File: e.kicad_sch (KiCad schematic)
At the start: 10 parts, among them SW1 usr, SW2 rst, U1 Display_ST7789, U2 MAX98357A

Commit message: Updated footprint library path for custom footprints
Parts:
- LS1: footprint stupid-dumb-speaker:stupid-dumb-speaker -> custom-fp:stupid-dumb-speaker
- U1: footprint display-lol:display-lol -> custom-fp:display-lol
- U2: footprint amp-of-doom:MAX98357A -> custom-fp:MAX98357A
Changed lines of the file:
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@@
 			)
 		)
-		(property "Footprint" "stupid-dumb-speaker:stupid-dumb-speaker"
+		(property "Footprint" "custom-fp:stupid-dumb-speaker"
 			(at 163.83 147.32 0)
 			(hide yes)
@@
 			)
 		)
-		(property "Footprint" "amp-of-doom:MAX98357A"
+		(property "Footprint" "custom-fp:MAX98357A"
 			(at 140.97 152.4 0)
 			(hide yes)
@@
 			)
 		)
-		(property "Footprint" "display-lol:display-lol"
+		(property "Footprint" "custom-fp:display-lol"
 			(at 92.71 93.98 0)
 			(hide yes)

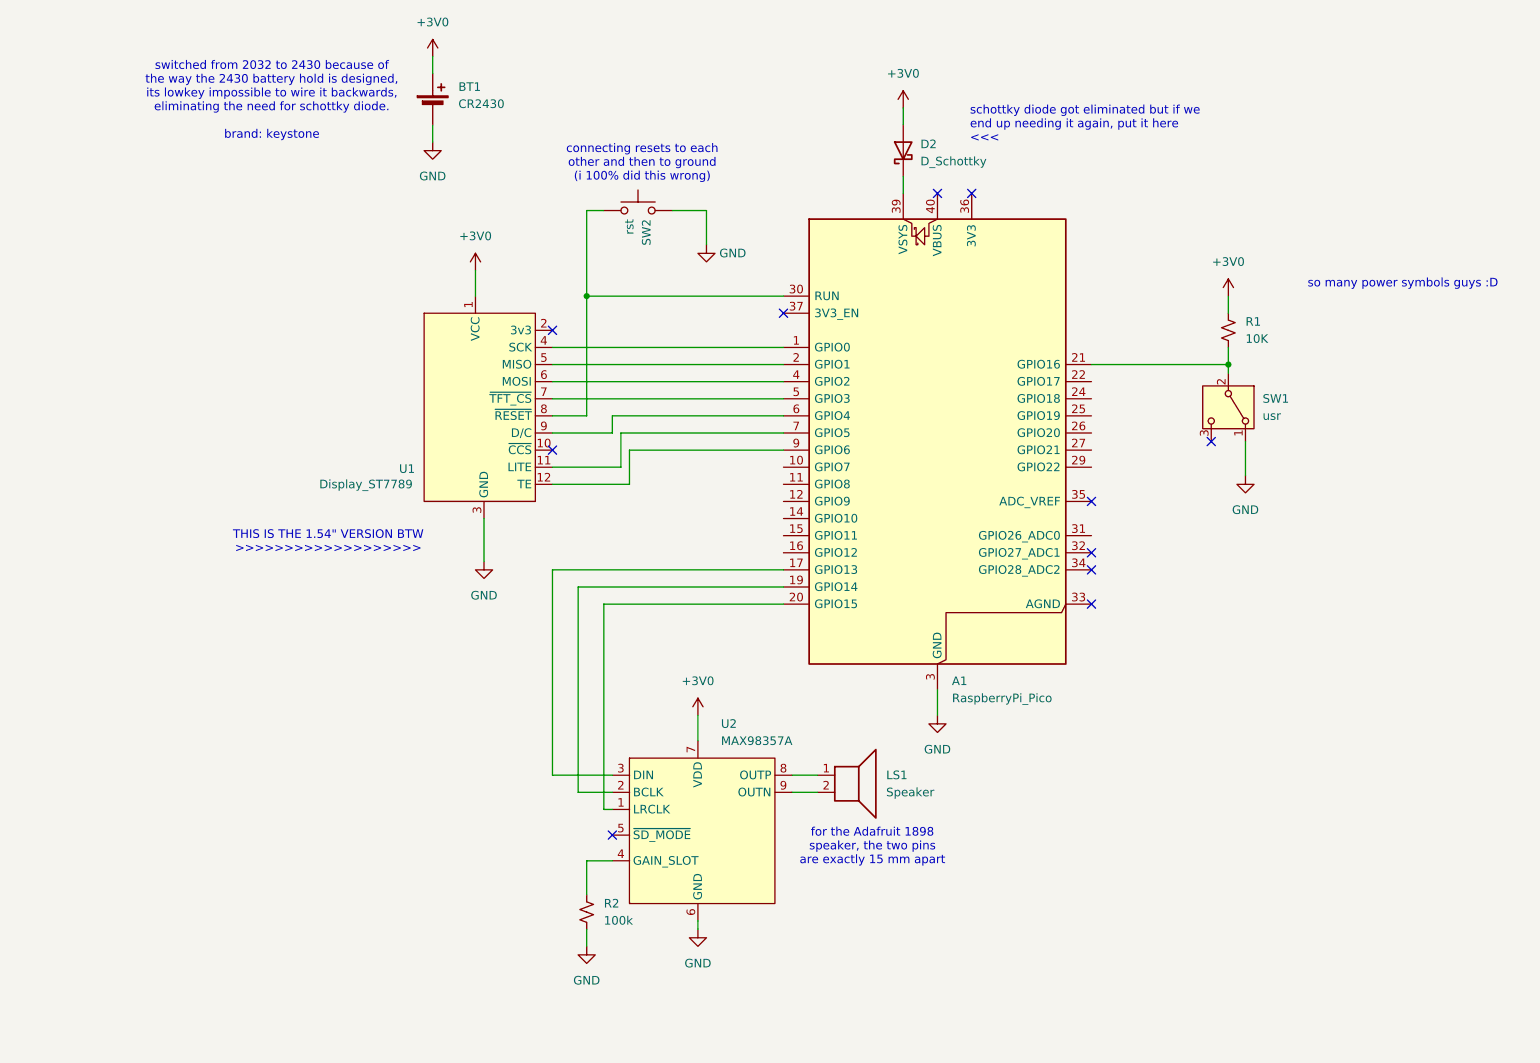
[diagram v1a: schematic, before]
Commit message: fixed some ERC/DRC errors
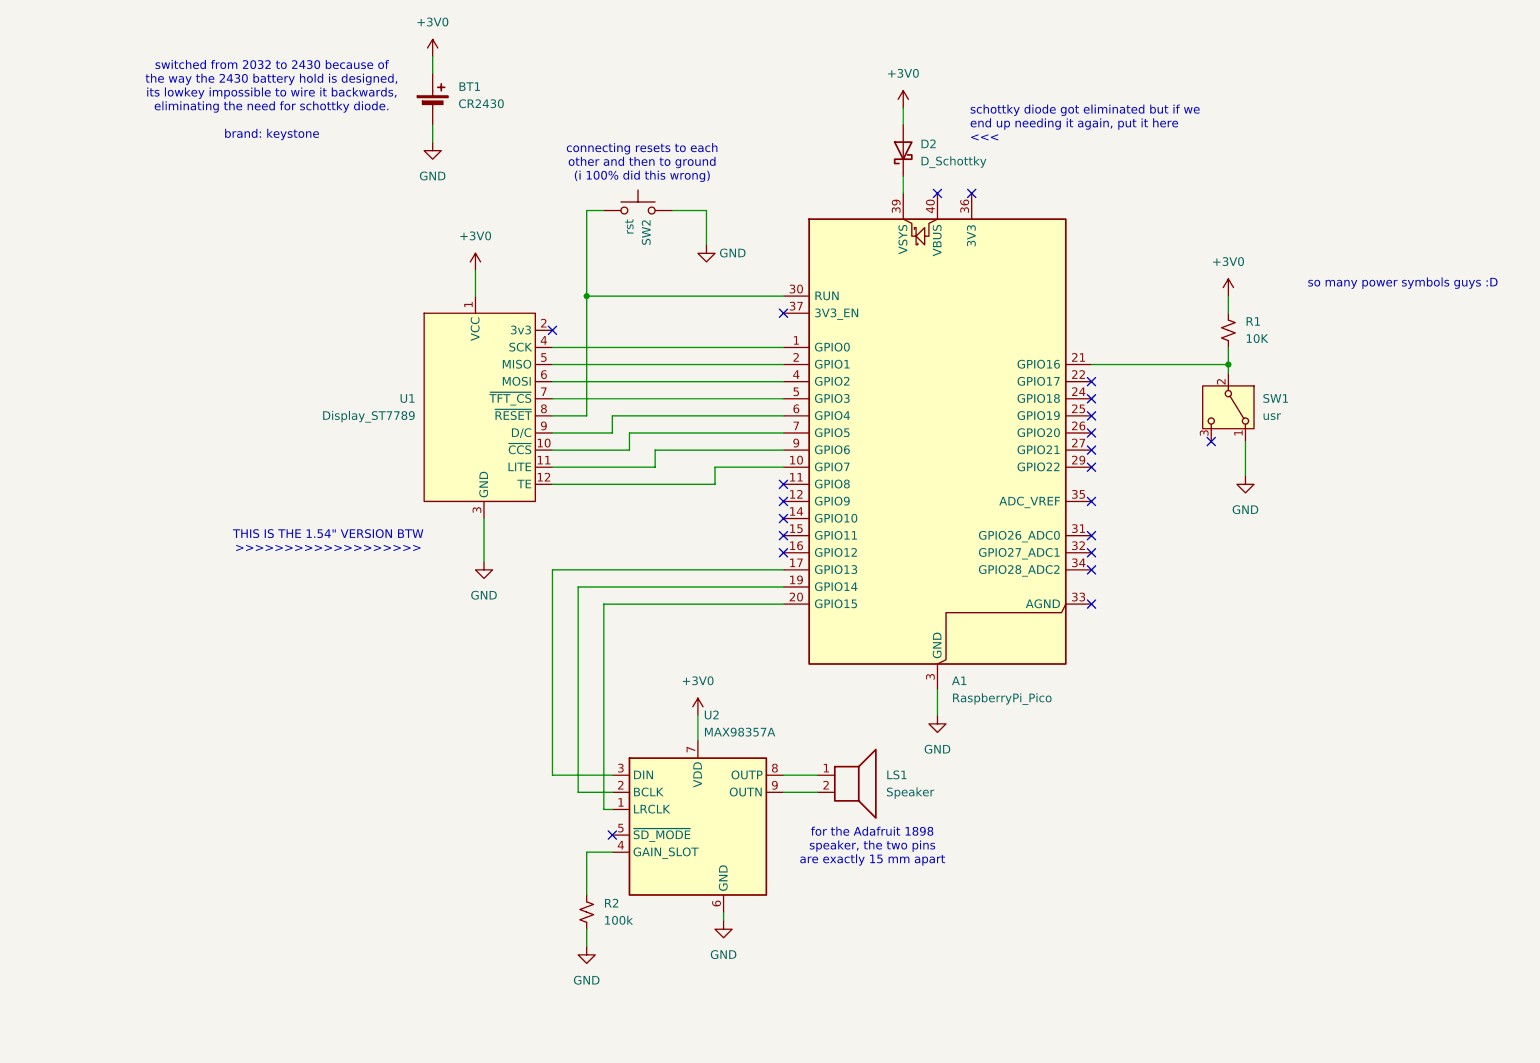
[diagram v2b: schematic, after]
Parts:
- removed U1: Display_ST7789, custom-fp:display-lol, symbol display_idk_lol:small-display
- added U1: Display_ST7789, custom-fp:display-lol, symbol cool-stuff:small-display
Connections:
- net +3V0: now also U1.1 (VCC)
- net GND: now also U1.3 (GND)
- net at A1.1 (GPIO0): now also U1.4 (SCK)
- net at A1.10 (GPIO7): now also U1.12 (TE)
- net at A1.2 (GPIO1): now also U1.5 (MISO)
- net at A1.30 (RUN), SW2.1: now also U1.8 (~{RESET})
- net at A1.4 (GPIO2): now also U1.6 (MOSI)
- net at A1.5 (GPIO3): now also U1.7 (~{TFT_CS})
- net at A1.6 (GPIO4): now also U1.9 (D/C)
- net at A1.7 (GPIO5): now also U1.10 (~{CCS})
- net at A1.9 (GPIO6): now also U1.11 (LITE)
- no-connect marks 11 -> 22
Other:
- moved on the sheet: U2

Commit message: wowwwww
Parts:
- removed SW1: usr, Button_Switch_THT:SW_Slide_SPDT_Straight_CK_OS102011MS2Q, symbol Switch:SW_SPDT
- removed U1: Display_ST7789, custom-fp:display-lol, symbol cool-stuff:small-display
- added SW1: usr, Button_Switch_SMD:SW_SPST_B3S-1000, symbol Switch:SW_Push
- added U1: (no value), display-lol:display-lol, symbol display_idk_lol:small-display
- LS1: footprint custom-fp:stupid-dumb-speaker -> stupid-dumb-speaker:stupid-dumb-speaker
- U2: footprint custom-fp:MAX98357A -> Package_DFN_QFN:TQFN-16-1EP_3x3mm_P0.5mm_EP1.23x1.23mm
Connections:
- net +3V0: now also U2.8 (OUTP), U1.1 (VCC)
- net GND: now also SW2.1, U2.11 (GND), U2.15 (GND), SW1.2, U1.3 (GND); no longer SW2.2
- net at A1.20 (GPIO15): no longer U2.1 (LRCLK)
- net at A1.19 (GPIO14): no longer U2.2 (BCLK)
- net at U2.3 (DIN): now also A1.1 (GPIO0); no longer A1.17 (GPIO13)
- net at A1.2 (GPIO1): now also U2.2 (BCLK)
- net at A1.21 (GPIO16), R1.2: now also SW1.1
- net at A1.22 (GPIO17): now also U1.4 (SCK)
- net at A1.24 (GPIO18): now also U1.5 (MISO)
- net at A1.25 (GPIO19): now also U1.6 (MOSI)
- net at A1.26 (GPIO20): now also U1.7 (~{TFT_CS})
- net at A1.27 (GPIO21): now also U1.9 (D/C)
- net at A1.29 (GPIO22): now also U1.11 (LITE)
- net at A1.30 (RUN): now also SW2.2, U1.8 (~{RESET}); no longer SW2.1
- net at A1.4 (GPIO2): now also U2.1 (LRCLK)
- no-connect marks 22 -> 24
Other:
- note added: "THIS IS THE 1.54" VERSION BTW <<<<<<<<<<<<<<<<<<<"
- note removed: "THIS IS THE 1.54" VERSION BTW >>>>>>>>>>>>>>>>>>>"
- moved on the sheet: A1, BT1, D2, LS1, R1, R2

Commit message: omg yay pcb fully made and its amazing and beautiful and the DRC errors make no sense :3
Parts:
- removed SW1: usr, Button_Switch_SMD:SW_SPST_B3S-1000, symbol Switch:SW_Push
- added SW1: usr, Button_Switch_THT:SW_Slide_SPDT_Straight_CK_OS102011MS2Q, symbol Switch:SW_SPDT
- U1: value (none) -> Display_ST7789
- U2: footprint Package_DFN_QFN:TQFN-16-1EP_3x3mm_P0.5mm_EP1.23x1.23mm -> MAX98357A:MAX98357A
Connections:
- net +3V0: no longer U2.8 (OUTP)
- net GND: now also SW1.1 (A); no longer U2.11 (GND), U2.15 (GND)
- net at A1.21 (GPIO16), R1.2: now also SW1.2 (B)
- no-connect marks 24 -> 25

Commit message: fixed so many things (i hope)
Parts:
- U2: footprint MAX98357A:MAX98357A -> amp-of-doom:MAX98357A
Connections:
- net GND: now also SW2.2; no longer SW2.1
- net at U2.1 (LRCLK): now also A1.20 (GPIO15); no longer A1.4 (GPIO2)
- net at U2.2 (BCLK): now also A1.19 (GPIO14); no longer A1.2 (GPIO1)
- net at U2.3 (DIN): now also A1.17 (GPIO13); no longer A1.1 (GPIO0)
- net at U1.4 (SCK): now also A1.1 (GPIO0); no longer A1.22 (GPIO17)
- net at U1.5 (MISO): now also A1.2 (GPIO1); no longer A1.24 (GPIO18)
- net at A1.25 (GPIO19): no longer U1.6 (MOSI)
- net at A1.26 (GPIO20): no longer U1.7 (~{TFT_CS})
- net at A1.27 (GPIO21): no longer U1.9 (D/C)
- net at A1.29 (GPIO22): no longer U1.11 (LITE)
- net at A1.30 (RUN), U1.8 (~{RESET}): now also SW2.1; no longer SW2.2
- net at A1.5 (GPIO3): now also U1.7 (~{TFT_CS})
- net at A1.6 (GPIO4): now also U1.9 (D/C)
- net at A1.7 (GPIO5): now also U1.11 (LITE)
- net at A1.9 (GPIO6): now also U1.12 (TE)
- new net: A1.4 (GPIO2), U1.6 (MOSI)
- no-connect marks 25 -> 11
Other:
- note added: "THIS IS THE 1.54" VERSION BTW >>>>>>>>>>>>>>>>>>>"
- note removed: "THIS IS THE 1.54" VERSION BTW <<<<<<<<<<<<<<<<<<<"
- moved on the sheet: A1, BT1, D2, LS1, R1, R2, SW1, U2
